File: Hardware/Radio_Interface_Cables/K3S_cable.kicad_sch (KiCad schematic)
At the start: 2 parts, among them J10 DE15_Socket_HighDensity, J6 RJ45

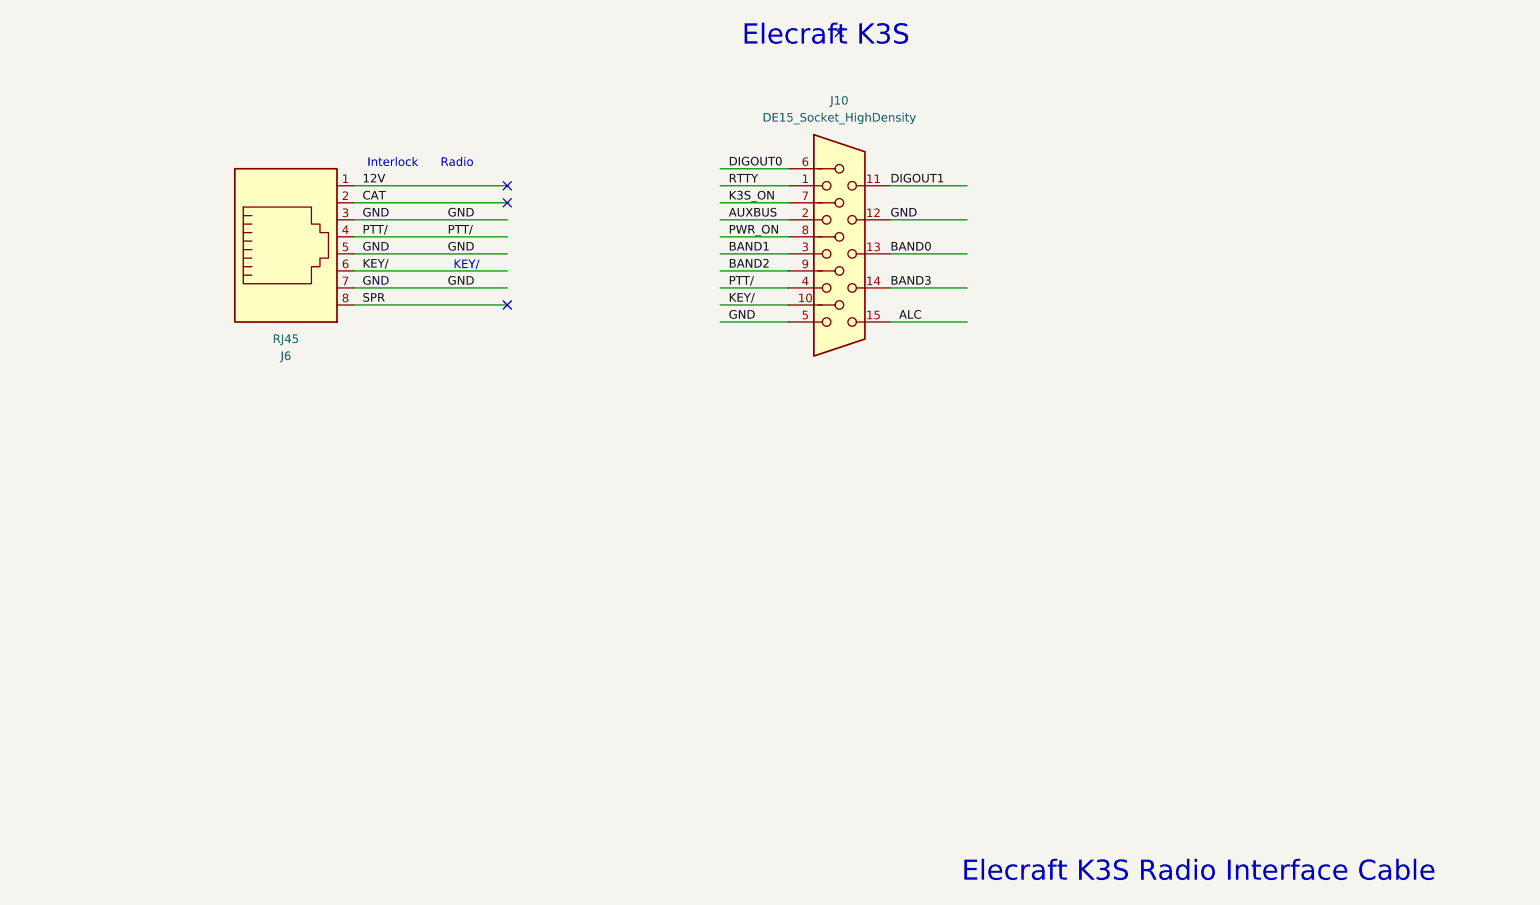
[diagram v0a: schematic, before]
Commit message: Add PTT and CAT connectors on Radio Interface Cables Mark pins as unused
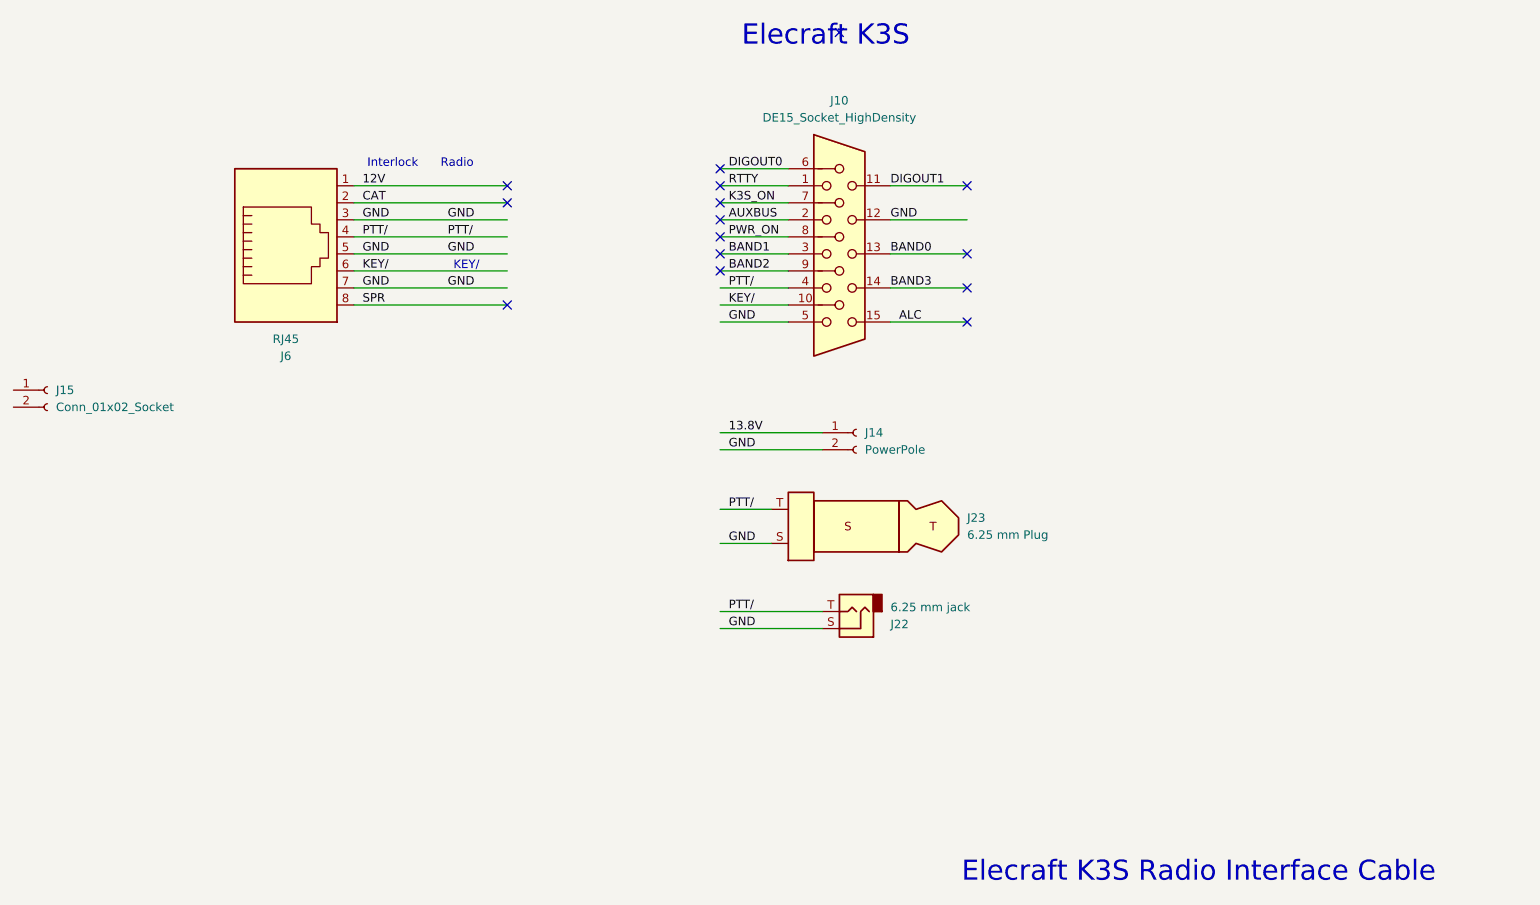
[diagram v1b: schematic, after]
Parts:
- added J14: PowerPole, symbol Connector:Conn_01x02_Socket
- added J15: Conn_01x02_Socket, symbol Connector:Conn_01x02_Socket
- added J22: 6.25 mm jack, symbol Connector_Audio:AudioJack2
- added J23: 6.25 mm Plug, symbol Connector_Audio:AudioPlug2
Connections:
- net GND: now also J14.2 (Pin_2), J22.S, J23.S
- net PTT/: now also J22.T, J23.T
- new net 13.8V: J14.1 (Pin_1)
- no-connect marks 4 -> 15

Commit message: Added LibreOffice Impress file describing design and use
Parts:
- removed J15: Conn_01x02_Socket, symbol Connector:Conn_01x02_Socket
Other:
- moved on the sheet: J6
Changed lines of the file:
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@@
 	(text "Elecraft K3S"
 		(exclude_from_sim no)
-		(at 165.608 48.768 0)
+		(at 165.608 53.848 0)
 		(effects
 			(font
@@
 	(text "Interlock      Radio"
 		(exclude_from_sim no)
-		(at 105.156 67.818 0)
+		(at 124.206 67.818 0)
 		(effects
 			(font
@@
 	(text "KEY/"
 		(exclude_from_sim no)
-		(at 112.014 83.058 0)
+		(at 131.064 83.058 0)
 		(effects
 			(font
@@
 	)
 	(no_connect
-		(at 118.11 88.9)
+		(at 137.16 88.9)
 	)
 	(no_connect
@@
 	)
 	(no_connect
-		(at 118.11 73.66)
+		(at 137.16 73.66)
 	)
 	(no_connect
@@
 	)
 	(no_connect
-		(at 167.64 48.26)
+		(at 167.64 53.34)
 	)
 	(no_connect
-		(at 118.11 71.12)
+		(at 137.16 71.12)
 	)
 	(no_connect
@@
 	(wire
 		(pts
-			(xy 95.25 83.82) (xy 118.11 83.82)
+			(xy 114.3 83.82) (xy 137.16 83.82)
 		)
 		(stroke
@@
 	(wire
 		(pts
-			(xy 95.25 71.12) (xy 118.11 71.12)
-		)
-		(stroke
-			(width 0)
-			(type default)
-		)
-	)
-	(wire
-		(pts
-			(xy 95.25 76.2) (xy 118.11 76.2)
+			(xy 114.3 71.12) (xy 137.16 71.12)
+		)
+		(stroke
+			(width 0)
+			(type default)
+		)
+	)
+	(wire
+		(pts
+			(xy 114.3 76.2) (xy 137.16 76.2)
 		)
 		(stroke
@@
 	(wire
 		(pts
-			(xy 95.25 81.28) (xy 118.11 81.28)
+			(xy 114.3 81.28) (xy 137.16 81.28)
 		)
 		(stroke
@@
 	(wire
 		(pts
-			(xy 95.25 73.66) (xy 118.11 73.66)
+			(xy 114.3 73.66) (xy 137.16 73.66)
 		)
 		(stroke
@@
 	(wire
 		(pts
-			(xy 95.25 86.36) (xy 118.11 86.36)
-		)
-		(stroke
-			(width 0)
-			(type default)
-		)
-	)
-	(wire
-		(pts
-			(xy 95.25 78.74) (xy 118.11 78.74)
+			(xy 114.3 86.36) (xy 137.16 86.36)
+		)
+		(stroke
+			(width 0)
+			(type default)
+		)
+	)
+	(wire
+		(pts
+			(xy 114.3 78.74) (xy 137.16 78.74)
 		)
 		(stroke
@@
 	(wire
 		(pts
-			(xy 95.25 88.9) (xy 118.11 88.9)
+			(xy 114.3 88.9) (xy 137.16 88.9)
 		)
 		(stroke
@@
 	)
 	(image
-		(at 57.785 78.105)
+		(at 76.835 78.105)
 		(scale 1.14669)
 		(data "iVBORw0KGgoAAAANSUhEUgAAAXkAAAEJCAYAAABxIVf8AAAABHNCSVQICAgIfAhkiAAAABl0RVh0"
@@
 	)
 	(label "GND"
-		(at 96.52 76.2 0)
+		(at 115.57 76.2 0)
 		(effects
 			(font
@@
 	)
 	(label "SPR"
-		(at 96.52 88.9 0)
+		(at 115.57 88.9 0)
 		(effects
 			(font
@@
 	)
 	(label "PTT{slash}"
-		(at 96.52 78.74 0)
+		(at 115.57 78.74 0)
 		(effects
 			(font
@@
 	)
 	(label "GND"
-		(at 109.22 86.36 0)
+		(at 128.27 86.36 0)
 		(effects
 			(font
@@
 	)
 	(label "GND"
-		(at 96.52 81.28 0)
+		(at 115.57 81.28 0)
 		(effects
 			(font
@@
 	)
 	(label "GND"
-		(at 109.22 81.28 0)
+		(at 128.27 81.28 0)
 		(effects
 			(font
@@
 	)
 	(label "PTT{slash}"
-		(at 109.22 78.74 0)
+		(at 128.27 78.74 0)
 		(effects
 			(font
@@
 	)
 	(label "GND"
-		(at 109.22 76.2 0)
+		(at 128.27 76.2 0)
 		(effects
 			(font
@@
 	)
 	(label "12V"
-		(at 96.52 71.12 0)
+		(at 115.57 71.12 0)
 		(effects
 			(font
@@
 	)
 	(label "KEY{slash}"
-		(at 96.52 83.82 0)
+		(at 115.57 83.82 0)
 		(effects
 			(font
@@
 	)
 	(label "CAT"
-		(at 96.52 73.66 0)
+		(at 115.57 73.66 0)
 		(effects
 			(font
@@
 	)
 	(label "GND"
-		(at 96.52 86.36 0)
+		(at 115.57 86.36 0)
 		(effects
 			(font
@@
 			)
 			(justify left bottom)
-		)
-	)
-	(symbol
-		(lib_id "Connector:Conn_01x02_Socket")
-		(at 49.53 101.6 0)
-		(unit 1)
-		(exclude_from_sim no)
-		(in_bom yes)
-		(on_board yes)
-		(dnp no)
-		(fields_autoplaced yes)
-		(property "Reference" "J15"
-			(at 50.8 101.5999 0)
-			(effects
-				(font
-					(size 1.27 1.27)
-				)
-				(justify left)
-			)
-		)
-		(property "Value" "Conn_01x02_Socket"
-			(at 50.8 104.1399 0)
-			(effects
-				(font
-					(size 1.27 1.27)
-				)
-				(justify left)
-			)
-		)
-		(property "Footprint" ""
-			(at 49.53 101.6 0)
-			(effects
-				(font
-					(size 1.27 1.27)
-				)
-				(hide yes)
-			)
-		)
-		(property "Datasheet" "~"
-			(at 49.53 101.6 0)
-			(effects
-				(font
-					(size 1.27 1.27)
-				)
-				(hide yes)
-			)
-		)
-		(property "Description" "Generic connector, single row, 01x02, script generated"
-			(at 49.53 101.6 0)
-			(effects
-				(font
-					(size 1.27 1.27)
-				)
-				(hide yes)
-			)
-		)
-		(pin "1"
-		)
-		(pin "2"
-		)
-		(instances
-			(project ""
-				(path "/65a6842f-7ce8-4a1d-bd27-c5cbbec442dc/581af204-107c-47d6-980c-6156cf0eb65e"
-					(reference "J15")
-					(unit 1)
-				)
-			)
 		)
 	)
@@
 	(symbol
 		(lib_id "Connector:RJ45")
-		(at 85.09 78.74 0)
+		(at 104.14 78.74 0)
 		(mirror x)
 		(unit 1)
@@
 		(dnp no)
 		(property "Reference" "J6"
-			(at 85.09 96.52 0)
+			(at 104.14 96.52 0)
 			(effects
 				(font
@@
 		)
 		(property "Value" "RJ45"
-			(at 85.09 93.98 0)
+			(at 104.14 93.98 0)
 			(effects
 				(font
@@
 		)
 		(property "Footprint" ""
-			(at 85.09 79.375 90)
+			(at 104.14 79.375 90)
 			(effects
 				(font
@@
 		)
 		(property "Datasheet" "~"
-			(at 85.09 79.375 90)
+			(at 104.14 79.375 90)
 			(effects
 				(font
@@
 		)
 		(property "Description" "RJ connector, 8P8C (8 positions 8 connected)"
-			(at 85.09 78.74 0)
+			(at 104.14 78.74 0)
 			(effects
 				(font
